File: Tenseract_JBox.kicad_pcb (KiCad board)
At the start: 2 copper layers, 63 x 24 mm, 19 parts, among them J1 MR30PW-M, J10 Conn_01x04_Pin, J11 Conn_01x04_Pin, J12 Conn_01x04_Pin, J15 TEST_IN, J16 TEST_OUT, J17 DO_SEL, J19 DO_SEL, J2 WS2815_01_IN, J3 WS2815_02_IN, J4 MR30PW-FB, J5 WS2815_01_OUT, J6 WS2815_02_OUT, J8 Conn_01x04_Pin

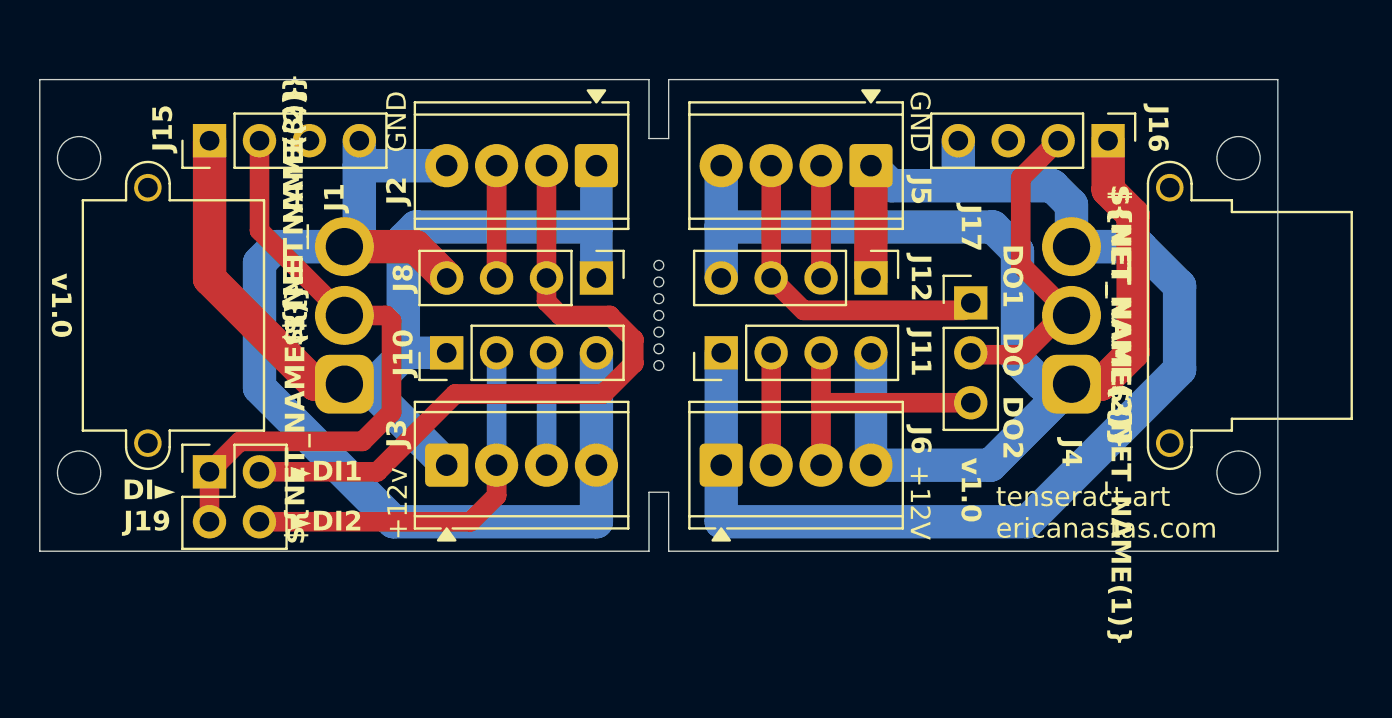
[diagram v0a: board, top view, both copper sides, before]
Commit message: moved mountiong holes in 0.5mm
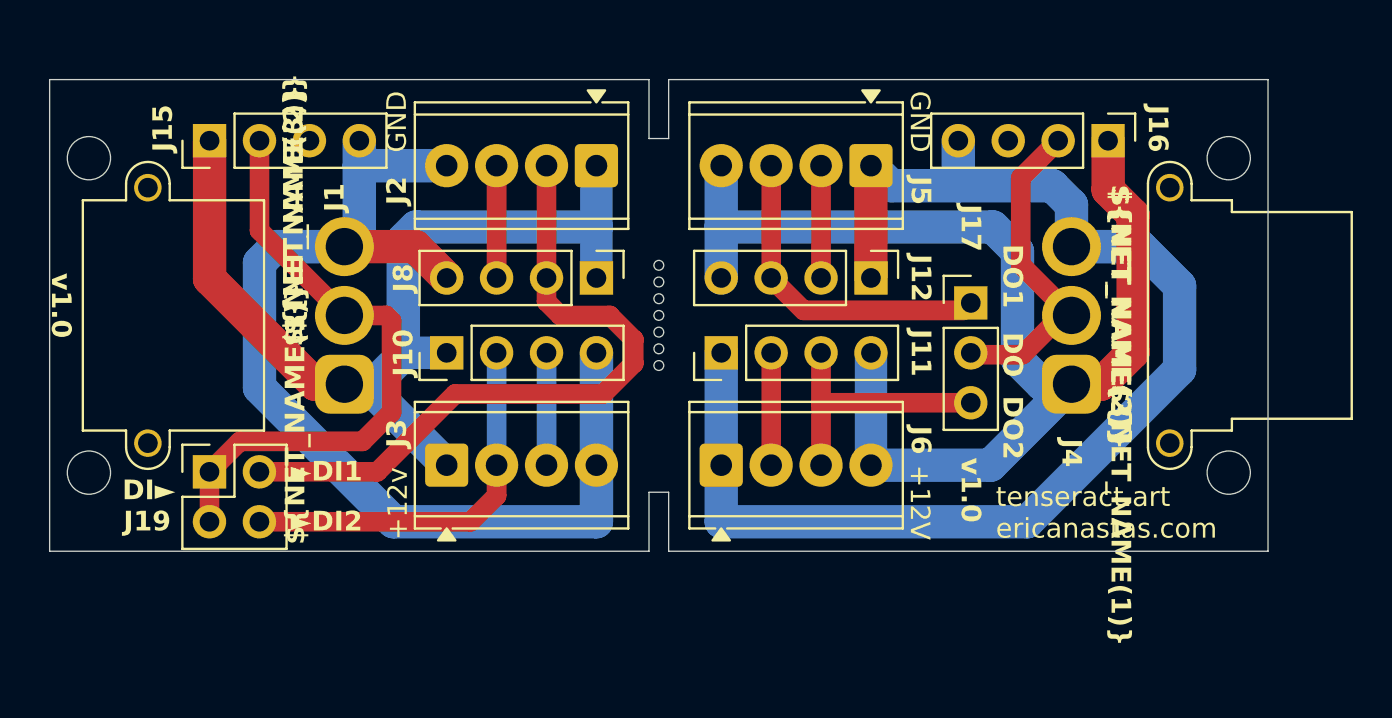
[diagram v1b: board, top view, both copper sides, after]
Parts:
- moved REF** 0.50 mm to (140.0, 58.0)
- moved REF** 0.50 mm to (82.0, 58.0)
- moved REF** 0.50 mm to (140.0, 42.0)
- moved REF** 0.50 mm to (82.0, 42.0)
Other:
- board size 63 x 24 mm -> 62 x 24 mm

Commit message: Finished 2nd pcb
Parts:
- added J15: DO_SEL2, Connector_PinHeader_2.54mm:PinHeader_1x03_P2.54mm_Vertical, F.Cu at (118.6, 53.8)
- J14: renamed from J17; value DO_SEL -> DO_SEL1
- moved J7 20.0 mm to (105.9, 48.7)
- moved J6 18.0 mm to (100.8, 53.8), turned to 180 degrees
- moved J13 15.1 mm to (125.6, 53.8), turned to 180 degrees
- moved J11 11.1 mm to (125.0, 60.2)
- moved J2 11.1 mm to (97.0, 39.8)
- moved J4 11.1 mm to (89.4, 60.2)
- moved J9 11.1 mm to (132.6, 39.8)
- moved J14 8.84 mm to (118.6, 46.2), turned to -90 degrees
- moved J10 7.01 mm to (121.2, 41.1)
- moved J5 7.01 mm to (100.8, 58.9)
- moved J12 7.01 mm to (113.5, 58.9)
- moved J3 7.01 mm to (108.5, 41.1)
- moved J1 1.00 mm to (96.0, 53.5)
- moved J8 1.00 mm to (131.0, 53.5)
- moved REF** 1.00 mm to (139.0, 58.0)
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- renumbered J12 to J10, J6 to J11, J11 to J12, J16 to J13, J8 to J3, J3 to J4, J10 to J5, J15 to J6, J19 to J7, J4 to J8, J5 to J9
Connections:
- net BI1 renamed /BI1
- net BO2 renamed /BO2
- net DI renamed /DI
- net DI2 renamed /DI2
- net DO renamed /DO
- J10 pad 2: B01 -> /BO1
- J10 pad 3: DO1 -> /DO1
- J11 pad 3: DO2 -> /DO2
- J12 pad 3: DO2 -> /DO2
- J14 pad 1: DO1 -> /BO1
- J14 pad 3: DO2 -> /DO1
- J9 pad 2: B01 -> /BO1
- J9 pad 3: DO1 -> /DO1
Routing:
- net /DO1: track 0.00 -> 22.6 mm
- net /DO2: track 0.00 -> 21.6 mm
- net /BO1: track 0.00 -> 21.6 mm
- net /DI: track 30.9 -> 13.0 mm
- net /BO2: track 5.71 -> 22.6 mm
- net DO1: track 16.7 -> 0.00 mm
- net DO2: track 13.4 -> 0.00 mm
- net /BI2: track 5.71 -> 16.6 mm
- net /BI1: track 5.71 -> 16.6 mm
- net /DI1: track 34.7 -> 25.2 mm
- net /DI2: track 19.9 -> 28.6 mm
- net /DO: track 16.7 -> 23.6 mm
- net B01: track 5.71 -> 0.00 mm
- net GND: track 122.5 -> 119.6 mm
- net +12V: track 113.4 -> 115.1 mm
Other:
- board size 62 x 24 mm -> 61 x 27 mm
- board text added: "12V"
- board text added: "BI"
- board text added: "BO"
- board text added: "BO1"
- board text added: "BO2"
- board text added: "DI"
- board text added: "ericanastas.com"
- board text added: "tenseract.art"
- board text removed: "+12v"
- board text removed: "DI►"
- board text removed: "tenseract.art ericanastas.com"
- board text removed: "►DI1"
- board text removed: "►DI2"

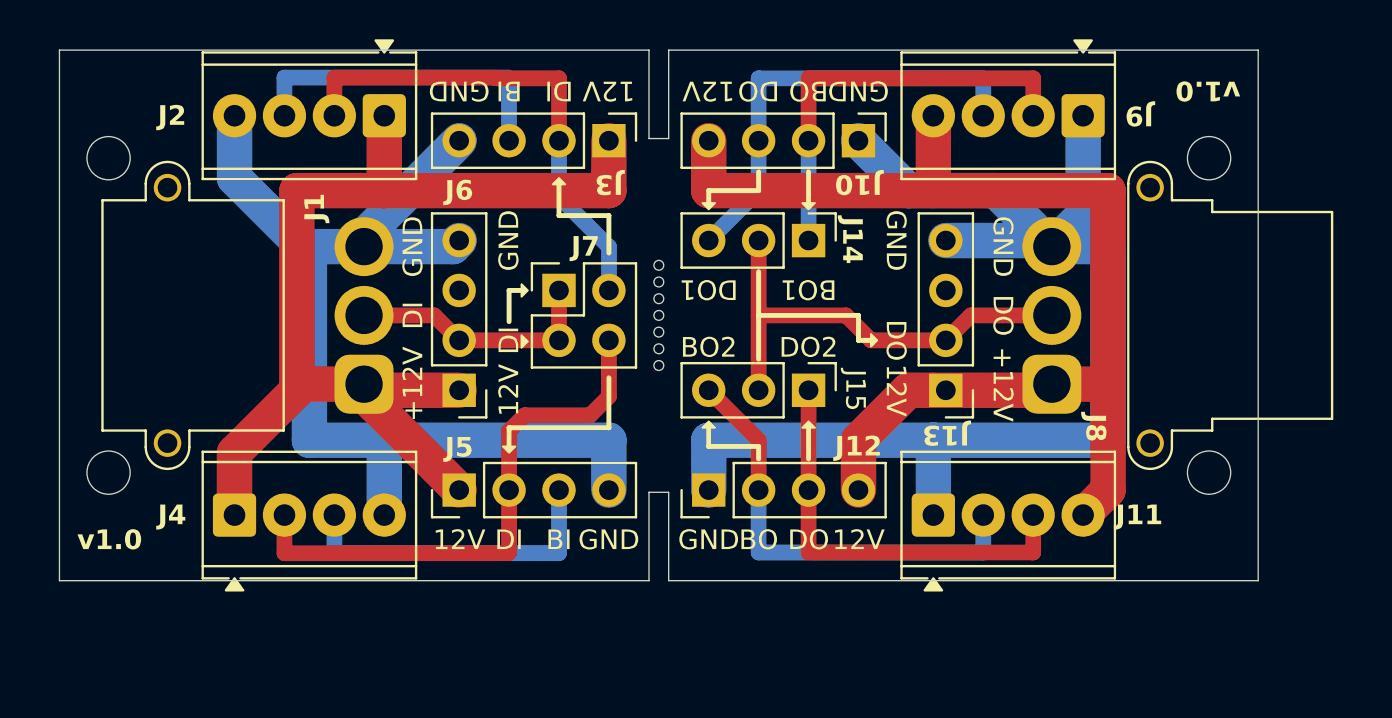
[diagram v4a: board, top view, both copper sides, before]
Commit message: Fixed mouse bites
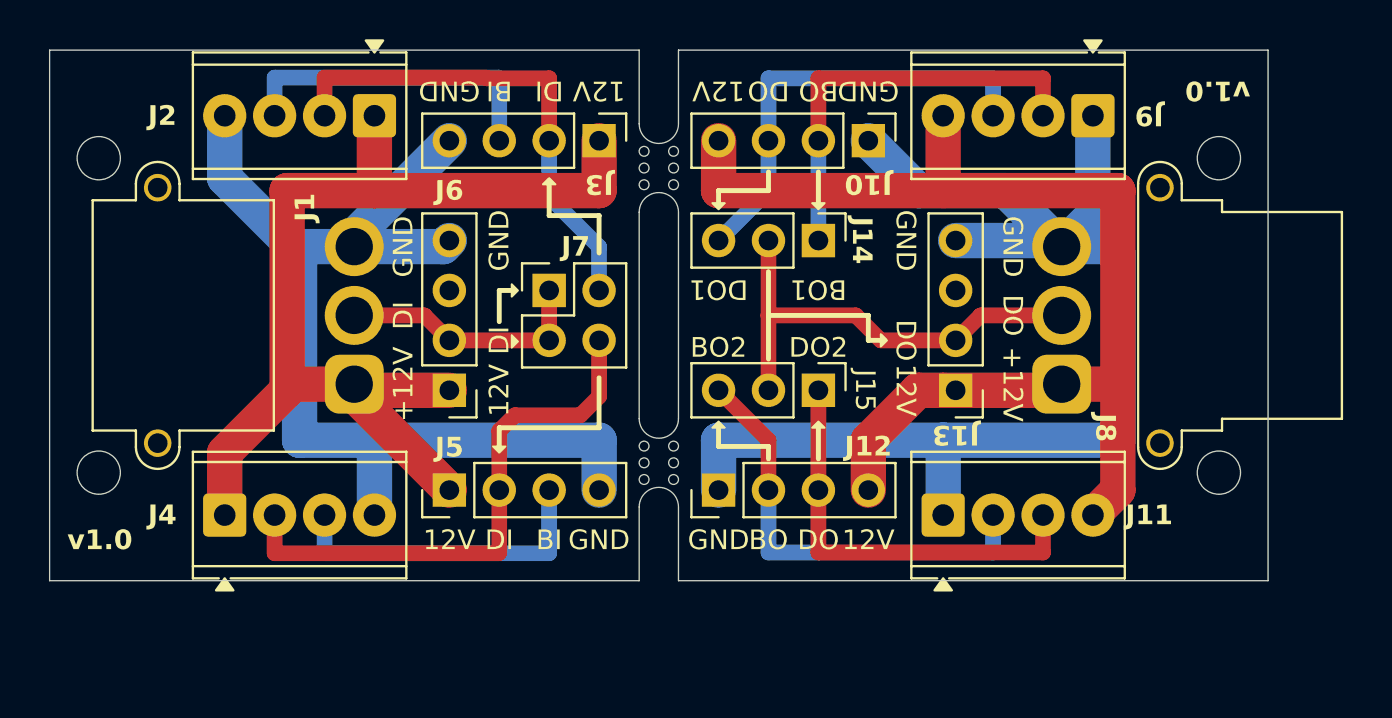
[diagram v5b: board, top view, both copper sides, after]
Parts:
- removed the REF** at (111.0, 50.0)
- added REF**: BreakLine_3h_D0.5mm_P0.85mm, Panelization:BreakLine_3h_D0.5mm_P0.85mm, F.Cu at (111.8, 42.5)
- added REF**: BreakLine_3h_D0.5mm_P0.85mm, Panelization:BreakLine_3h_D0.5mm_P0.85mm, F.Cu at (110.2, 42.5)
- added REF**: BreakLine_3h_D0.5mm_P0.85mm, Panelization:BreakLine_3h_D0.5mm_P0.85mm, F.Cu at (110.2, 57.5)
- added REF**: BreakLine_3h_D0.5mm_P0.85mm, Panelization:BreakLine_3h_D0.5mm_P0.85mm, F.Cu at (111.8, 57.5)
- moved J1 0.50 mm to (95.5, 53.5)
- moved J10 0.50 mm to (121.7, 41.1)
- moved J11 0.50 mm to (125.5, 60.2)
- moved J12 0.50 mm to (114.0, 58.9)
- moved J13 0.50 mm to (126.1, 53.8)
- moved J14 0.50 mm to (119.1, 46.2)
- moved J15 0.50 mm to (119.1, 53.8)
- moved J2 0.50 mm to (96.5, 39.8)
- moved J3 0.50 mm to (108.0, 41.1)
- moved J4 0.50 mm to (88.9, 60.2)
- moved J5 0.50 mm to (100.3, 58.9)
- moved J6 0.50 mm to (100.3, 53.8)
- moved J7 0.50 mm to (105.4, 48.7)
- moved J8 0.50 mm to (131.5, 53.5)
- moved J9 0.50 mm to (133.1, 39.8)
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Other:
- board size 61 x 27 mm -> 62 x 27 mm

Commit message: Removed JLCJLCJLCJLC placeholder
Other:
- board text added: "${TITLE} v${REVISION}"
- board text removed: "${TITLE} v${REVISION} ${CURRENT_DATE} JLCJLCJLCJLC"
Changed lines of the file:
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@@
 			(crossoutdnponfab yes)
 			(subtractmaskfromsilk no)
-			(outputformat 5)
+			(outputformat 1)
 			(mirror no)
 			(drillshape 0)
@@
 		)
 	)
-	(gr_text "${TITLE} v${REVISION} \n${CURRENT_DATE}\nJLCJLCJLCJLC\n"
-		(at 136 50 90)
+	(gr_text "${TITLE} v${REVISION}"
+		(at 139.5 50 90)
 		(layer "B.SilkS")
 		(effects
@@
 		)
 	)
-	(gr_text "${TITLE} v${REVISION}\n${CURRENT_DATE}\nJLCJLCJLCJLC"
-		(at 86 50 270)
+	(gr_text "${TITLE} v${REVISION}"
+		(at 82.5 50 270)
 		(layer "B.SilkS")
 		(effects
